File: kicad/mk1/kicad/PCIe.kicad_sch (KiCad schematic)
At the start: 23 parts, among them J13 Bus_M.2_Socket_M, U18 TLV62585DRLR

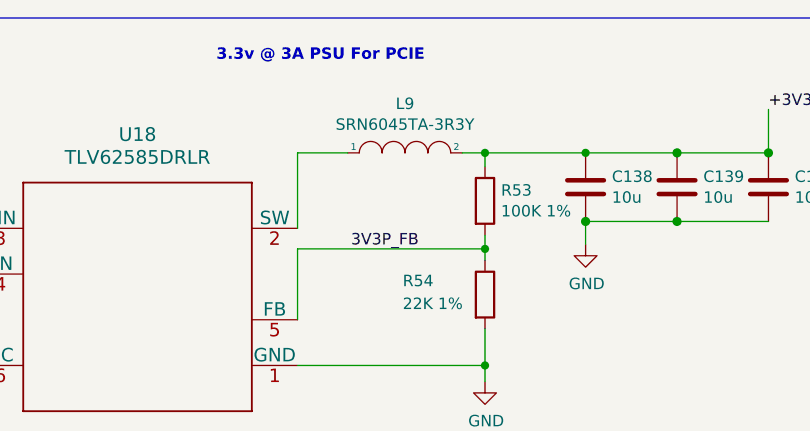
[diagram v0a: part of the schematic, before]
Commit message: work on schematics
* add power rail
* import CM4 related part
* design most of the BMC-PHY part
* create new library/footprint for rp t113-s3 SOM
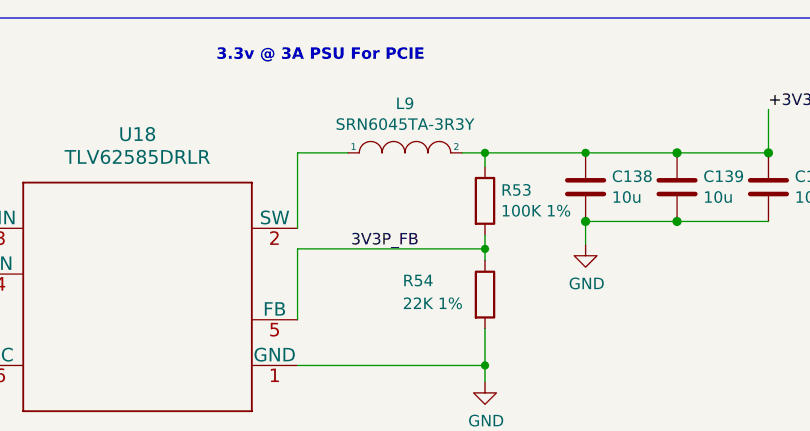
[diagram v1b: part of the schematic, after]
